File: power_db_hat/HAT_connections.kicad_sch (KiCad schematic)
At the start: 1 part, among them J8 GPIO

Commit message: update
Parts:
- renumbered J8 to J1
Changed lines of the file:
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@@
 		(on_board yes)
 		(dnp no)
-		(property "Reference" "#PWR032"
+		(property "Reference" "#PWR031"
 			(at 101.6 124.46 0)
 			(effects
@@
 			(project "power_db_hat"
 				(path "/e63e39d7-6ac0-4ffd-8aa3-1841a4541b55/74cd1f89-6647-48ce-abe4-db9e7a1a2a85"
-					(reference "#PWR032")
+					(reference "#PWR031")
 					(unit 1)
 				)
@@
 		(on_board yes)
 		(dnp no)
-		(property "Reference" "J8"
+		(property "Reference" "J1"
 			(at 110.49 60.5598 0)
 			(effects
@@
 			(project "power_db_hat"
 				(path "/e63e39d7-6ac0-4ffd-8aa3-1841a4541b55/74cd1f89-6647-48ce-abe4-db9e7a1a2a85"
-					(reference "J8")
+					(reference "J1")
 					(unit 1)
 				)
@@
 		(on_board yes)
 		(dnp no)
-		(property "Reference" "#PWR034"
+		(property "Reference" "#PWR033"
 			(at 119.38 124.46 0)
 			(effects
@@
 			(project "power_db_hat"
 				(path "/e63e39d7-6ac0-4ffd-8aa3-1841a4541b55/74cd1f89-6647-48ce-abe4-db9e7a1a2a85"
-					(reference "#PWR034")
+					(reference "#PWR033")
 					(unit 1)
 				)
@@
 		(on_board yes)
 		(dnp no)
-		(property "Reference" "#PWR031"
+		(property "Reference" "#PWR030"
 			(at 99.06 66.04 0)
 			(effects
@@
 			(project "power_db_hat"
 				(path "/e63e39d7-6ac0-4ffd-8aa3-1841a4541b55/74cd1f89-6647-48ce-abe4-db9e7a1a2a85"
-					(reference "#PWR031")
+					(reference "#PWR030")
 					(unit 1)
 				)
@@
 		(on_board yes)
 		(dnp no)
-		(property "Reference" "#PWR033"
+		(property "Reference" "#PWR032"
 			(at 119.38 66.04 0)
 			(effects
@@
 			(project "power_db_hat"
 				(path "/e63e39d7-6ac0-4ffd-8aa3-1841a4541b55/74cd1f89-6647-48ce-abe4-db9e7a1a2a85"
-					(reference "#PWR033")
-					(unit 1)
-				)
+					(reference "#PWR032")
+					(unit 1)
+				)

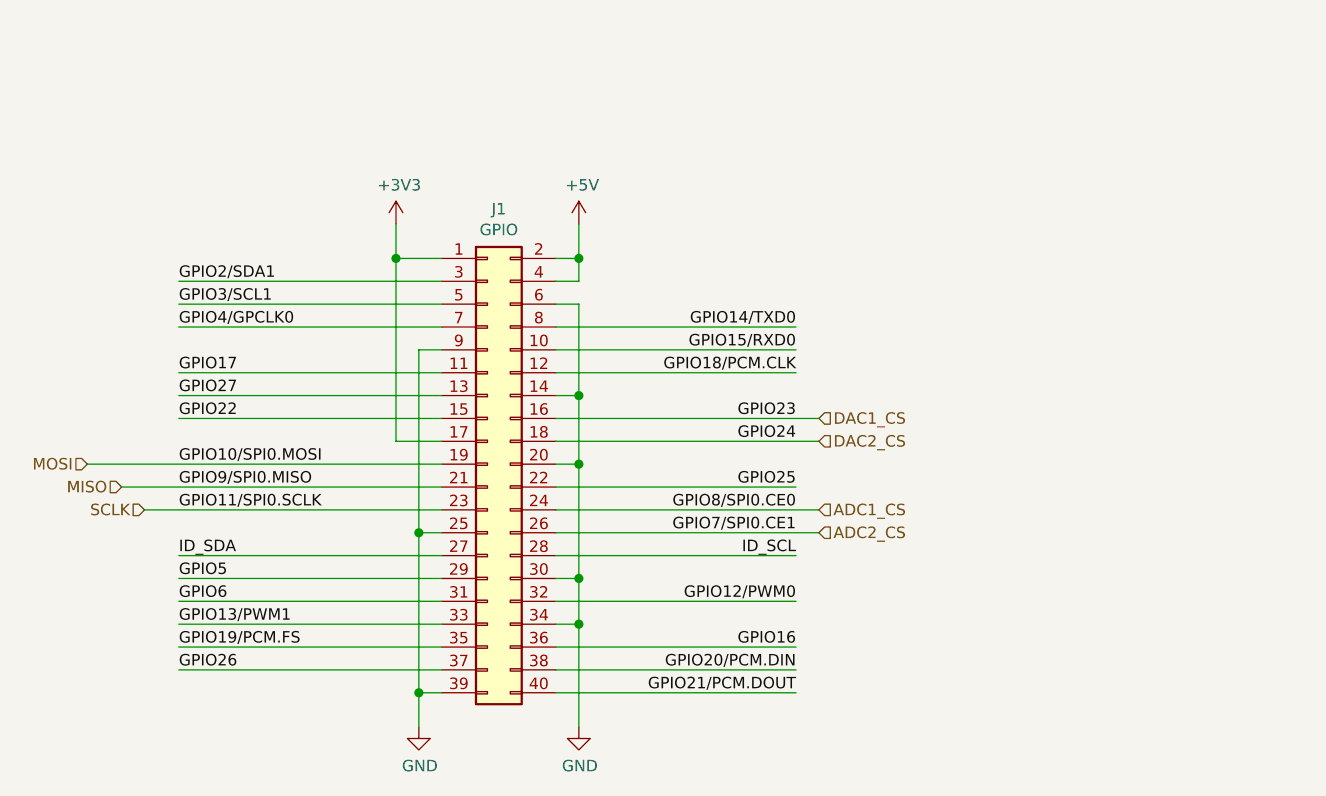
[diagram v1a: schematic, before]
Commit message: split into two PCBs
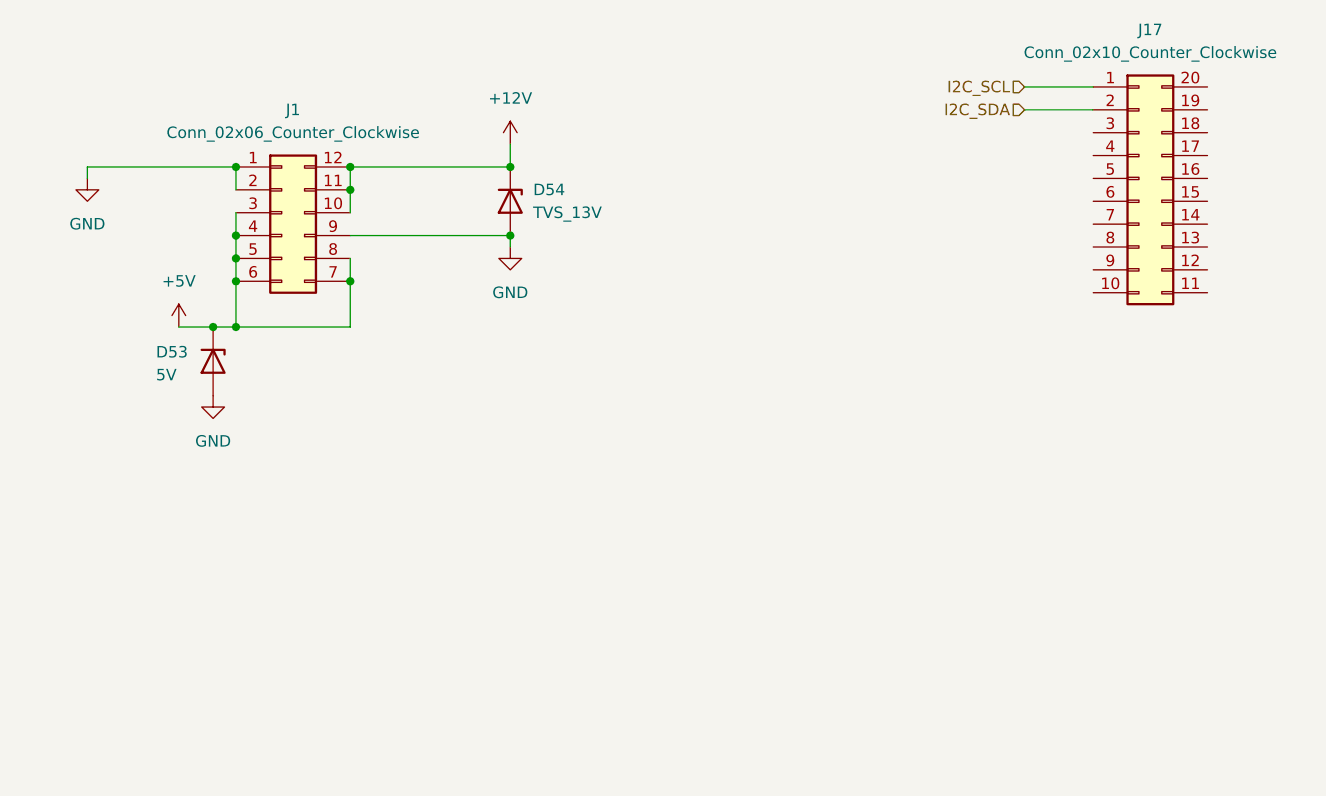
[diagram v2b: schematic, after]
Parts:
- removed J1: GPIO, Connector_PinSocket_2.54mm:PinSocket_2x20_P2.54mm_Vertical, symbol Connector_Generic:Conn_02x20_Odd_Even
- added D53: 5V, Diode_SMD:D_0603_1608Metric_Pad1.05x0.95mm_HandSolder, symbol Device:D_Zener
- added D54: TVS_13V, Diode_SMD:D_0603_1608Metric_Pad1.05x0.95mm_HandSolder, symbol Device:D_Zener
- added J1: Conn_02x06_Counter_Clockwise, Connector_PinHeader_2.54mm:PinHeader_2x06_P2.54mm_Vertical, symbol Connector_Generic:Conn_02x06_Counter_Clockwise
- added J17: Conn_02x10_Counter_Clockwise, Connector_PinHeader_2.54mm:PinHeader_2x10_P2.54mm_Vertical, symbol Connector_Generic:Conn_02x10_Counter_Clockwise
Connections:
- net +5V: now also D53.1 (K), J1.3 (Pin_3), J1.4 (Pin_4), J1.5 (Pin_5), J1.6 (Pin_6), J1.7 (Pin_7), J1.8 (Pin_8)
- net GND: now also D53.2 (A), D54.2 (A), J1.1 (Pin_1), J1.2 (Pin_2), J1.9 (Pin_9)
- new net +12V: D54.1 (K), J1.10 (Pin_10), J1.11 (Pin_11), J1.12 (Pin_12)
- new net I2C_SCL: J17.1 (Pin_1)
- new net I2C_SDA: J17.2 (Pin_2)

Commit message: LMAO
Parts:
- removed D53: 5V, Diode_SMD:D_0603_1608Metric_Pad1.05x0.95mm_HandSolder, symbol Device:D_Zener
- removed D54: TVS_13V, Diode_SMD:D_0603_1608Metric_Pad1.05x0.95mm_HandSolder, symbol Device:D_Zener
- removed J1: Conn_02x06_Counter_Clockwise, Connector_PinHeader_2.54mm:PinHeader_2x06_P2.54mm_Vertical, symbol Connector_Generic:Conn_02x06_Counter_Clockwise
- removed J17: Conn_02x10_Counter_Clockwise, Connector_PinHeader_2.54mm:PinHeader_2x10_P2.54mm_Vertical, symbol Connector_Generic:Conn_02x10_Counter_Clockwise

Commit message: lol
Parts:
- added D53: 5V, Diode_SMD:D_0603_1608Metric_Pad1.05x0.95mm_HandSolder, symbol Device:D_Zener
- added D54: TVS_13V, Diode_SMD:D_0603_1608Metric_Pad1.05x0.95mm_HandSolder, symbol Device:D_Zener
- added J1: Conn_02x06_Counter_Clockwise, Connector_PinHeader_2.54mm:PinHeader_2x06_P2.54mm_Vertical, symbol Connector_Generic:Conn_02x06_Counter_Clockwise
- added J17: Conn_02x10_Counter_Clockwise, Connector_PinHeader_2.54mm:PinHeader_2x10_P2.54mm_Vertical, symbol Connector_Generic:Conn_02x10_Counter_Clockwise
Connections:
- new net +12V: D54.1 (K), J1.10 (Pin_10), J1.11 (Pin_11), J1.12 (Pin_12)
- new net +5V: D53.1 (K), J1.3 (Pin_3), J1.4 (Pin_4), J1.5 (Pin_5), J1.6 (Pin_6), J1.7 (Pin_7), J1.8 (Pin_8)
- new net GND: D53.2 (A), D54.2 (A), J1.1 (Pin_1), J1.2 (Pin_2), J1.9 (Pin_9)
- new net I2C_SCL: J17.1 (Pin_1)
- new net I2C_SDA: J17.2 (Pin_2)

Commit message: lol
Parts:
- removed D53: 5V, Diode_SMD:D_0603_1608Metric_Pad1.05x0.95mm_HandSolder, symbol Device:D_Zener
- removed D54: TVS_13V, Diode_SMD:D_0603_1608Metric_Pad1.05x0.95mm_HandSolder, symbol Device:D_Zener
- removed J1: Conn_02x06_Counter_Clockwise, Connector_PinHeader_2.54mm:PinHeader_2x06_P2.54mm_Vertical, symbol Connector_Generic:Conn_02x06_Counter_Clockwise
- removed J17: Conn_02x10_Counter_Clockwise, Connector_PinHeader_2.54mm:PinHeader_2x10_P2.54mm_Vertical, symbol Connector_Generic:Conn_02x10_Counter_Clockwise
